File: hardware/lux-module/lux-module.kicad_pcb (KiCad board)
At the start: 2 copper layers, 6 parts, among them J1 Conn_01x04, U1 TSL25911FN

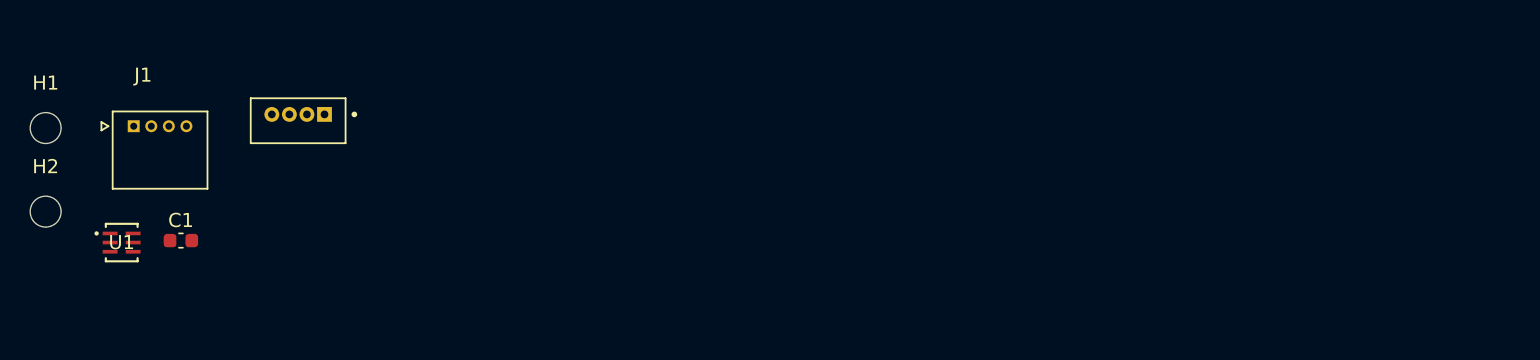
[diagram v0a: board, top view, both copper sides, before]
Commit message: finish lux moudle/ALS
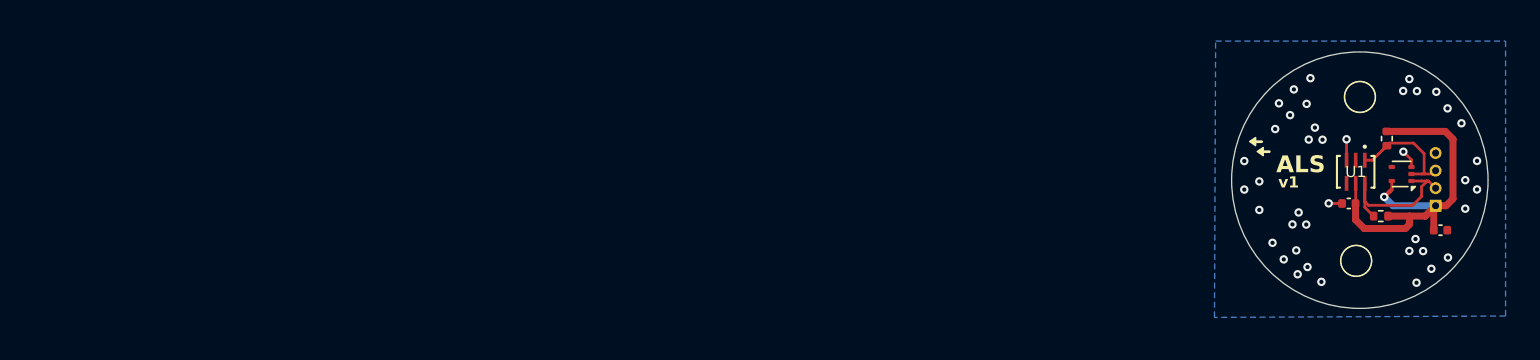
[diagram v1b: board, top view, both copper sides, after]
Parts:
- removed REF**: MOLEX_53047-0460, 53047-0460:MOLEX_53047-0460
- added C2: 10uF, Capacitor_SMD:C_0402_1005Metric, F.Cu at (139.0, 57.7)
- added R1: 2.2k, Resistor_SMD:R_0402_1005Metric, F.Cu at (134.7, 56.7)
- added R2: 2.2k, Resistor_SMD:R_0402_1005Metric, F.Cu at (135.2, 51.1)
- added U2: TPD3E001DRLR, Package_TO_SOT_SMD:SOT-553, F.Cu at (136.2, 53.7)
- C1: footprint Capacitor_SMD:C_0603_1608Metric -> Capacitor_SMD:C_0402_1005Metric
- J1: moved to B.Cu
- moved H2 93.9 mm to (133.2, 48.2)
- moved H1 93.8 mm to (133.0, 59.9)
- moved J1 92.8 mm to (138.6, 55.9), turned to 90 degrees
- moved U1 88.0 mm to (132.9, 53.5), turned to -90 degrees
- moved C1 83.2 mm to (132.4, 55.8), turned to 180 degrees
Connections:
- J1 pad 2: /SCL -> /SDA
- J1 pad 3: /SDA -> /SCL
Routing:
- net +3V3: track 0.00 -> 29.4 mm, vias 0 -> 1
- net /SDA: track 0.00 -> 11.5 mm
- net /SCL: track 0.00 -> 8.79 mm
- net GND: track 0.00 -> 3.78 mm, vias 0 -> 41
- added copper zone on B.Cu, net GND
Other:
- board outline added: 18.3 x 18.3 mm
- board text added: "2026"
- board text added: "ALS"
- board text added: "GND"
- board text added: "JS"
- board text added: "M2"
- board text added: "SCL"
- board text added: "SDA"
- board text added: "VCC"
- board text added: "homectrl"
- board text added: "v1"
- board text added: "|"

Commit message: power circuitry
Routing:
- net /SDA: track 11.5 -> 9.67 mm
- net GND: track 3.78 -> 4.63 mm, vias 41 -> 42
- added copper zone on F.Cu, net GND

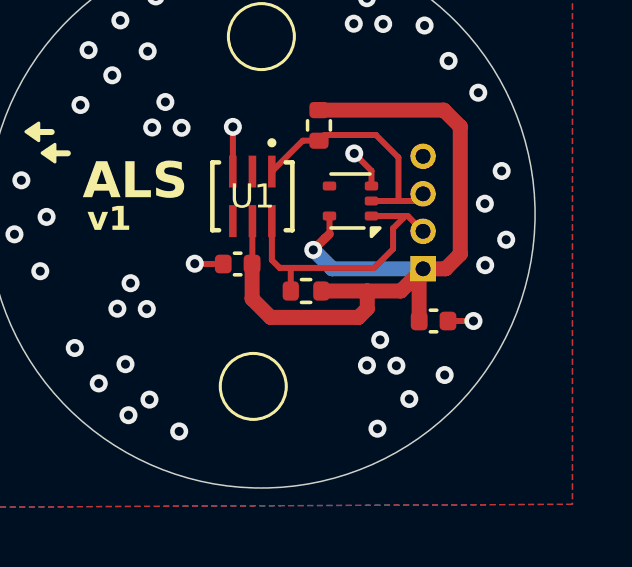
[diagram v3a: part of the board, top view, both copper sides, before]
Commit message: add new caps, add ferrite bead, add MPNs
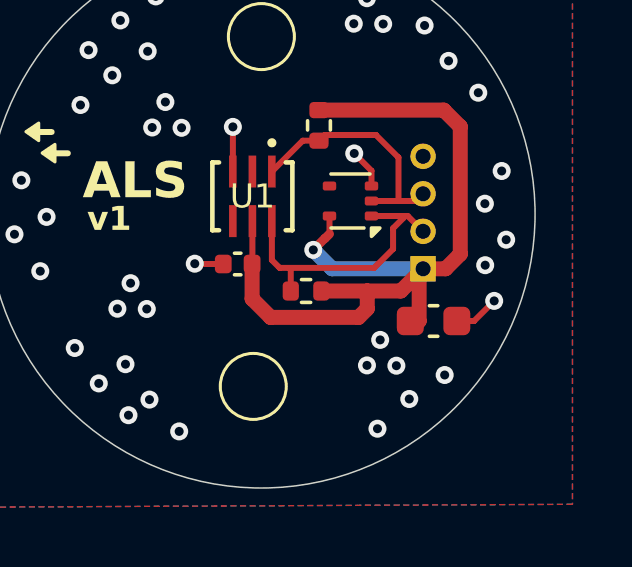
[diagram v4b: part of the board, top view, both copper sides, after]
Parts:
- C2: footprint Capacitor_SMD:C_0402_1005Metric -> Capacitor_SMD:C_0603_1608Metric
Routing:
- net GND: track 4.63 -> 5.59 mm

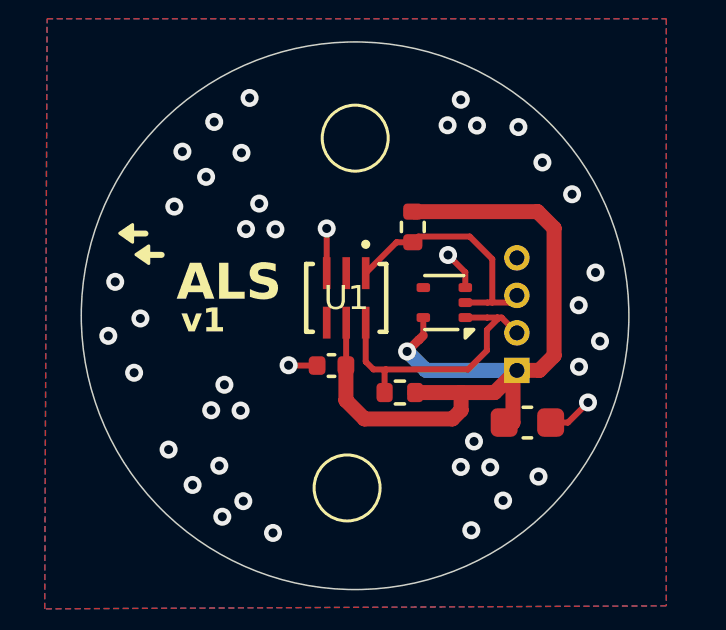
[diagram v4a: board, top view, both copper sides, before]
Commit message: add MPNs and review circuits
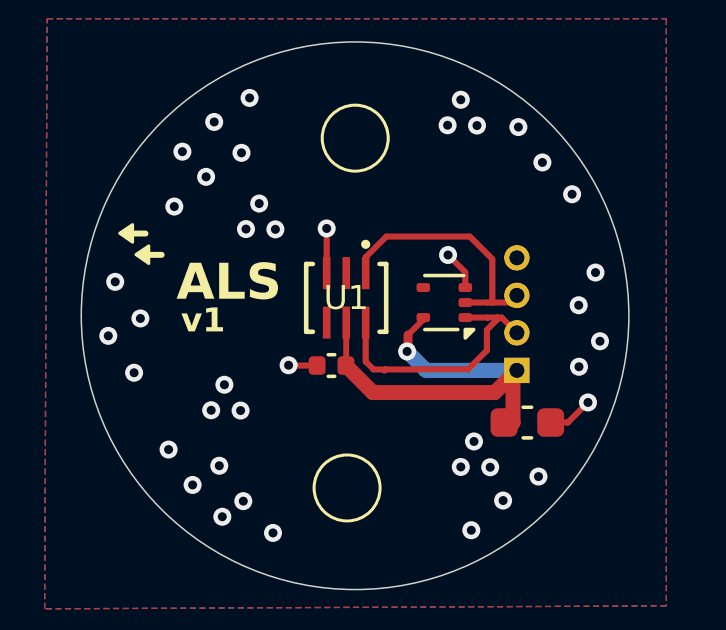
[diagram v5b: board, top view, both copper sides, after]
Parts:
- removed R1, R2: 2.2k, Resistor_SMD:R_0402_1005Metric
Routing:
- net +3V3: track 29.7 -> 15.2 mm
- net /SDA: track 9.67 -> 8.94 mm

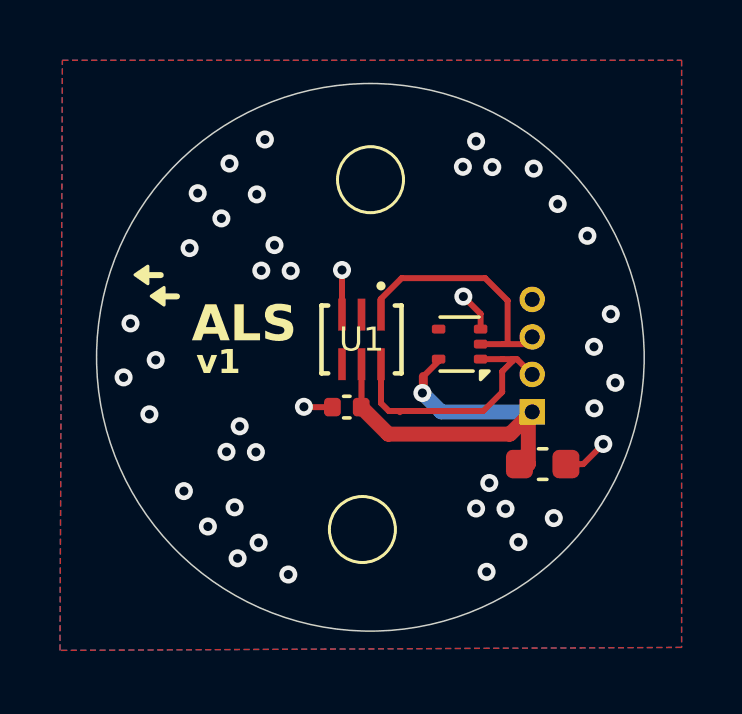
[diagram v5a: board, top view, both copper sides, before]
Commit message: review, add vias & ground pour
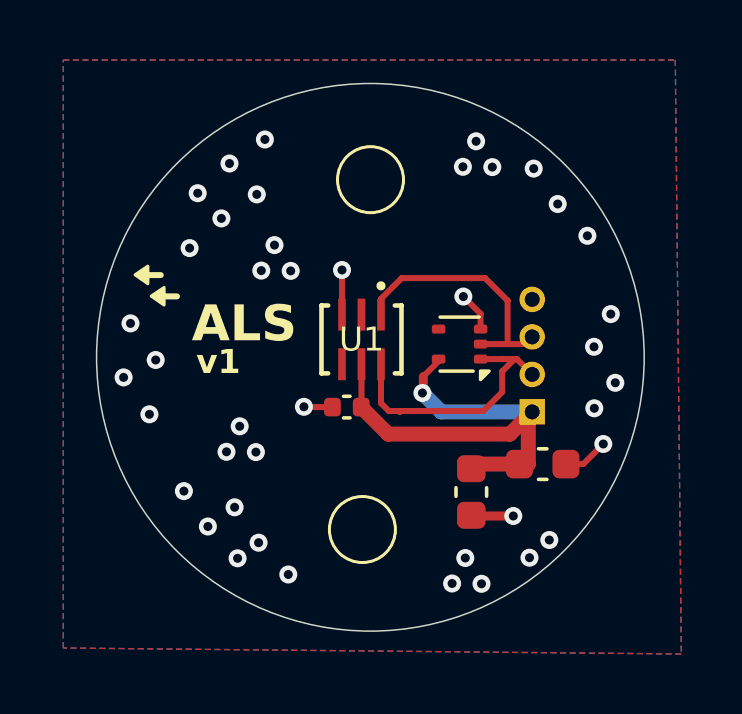
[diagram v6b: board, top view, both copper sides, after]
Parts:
- added Ce: 0.1uF, Capacitor_SMD:C_0603_1608Metric, F.Cu at (136.6, 58.6)
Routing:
- net +3V3: track 15.2 -> 16.9 mm
- net GND: track 5.59 -> 7.00 mm

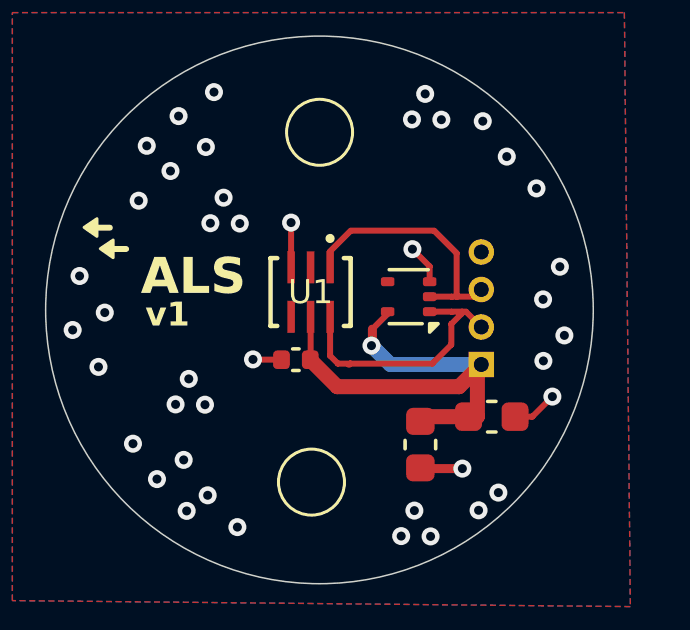
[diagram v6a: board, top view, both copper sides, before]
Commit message: pad clearance & BOM fixes
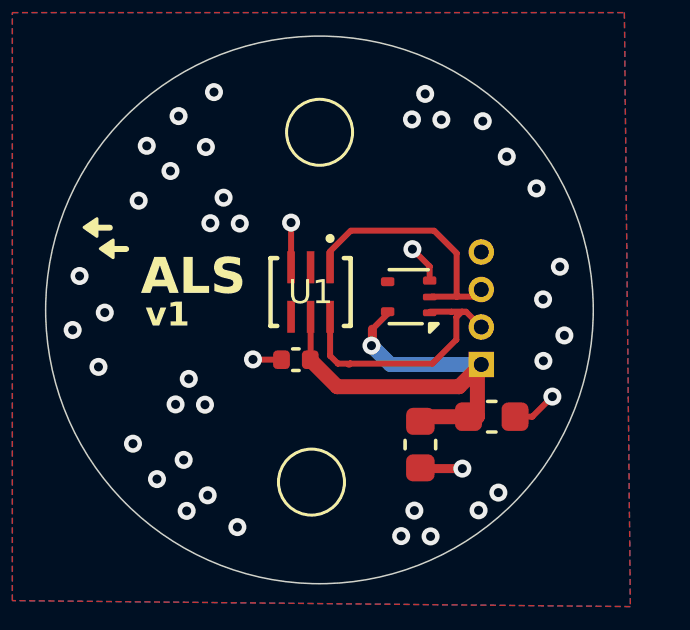
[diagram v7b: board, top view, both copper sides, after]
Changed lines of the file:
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@@
 		)
 		(pad "1" smd roundrect
-			(at -0.7 -0.5 180)
-			(size 0.45 0.3)
+			(at -0.7 -0.5375 180)
+			(size 0.45 0.225)
 			(layers "F.Cu" "F.Paste" "F.Mask")
 			(roundrect_rratio 0.25)
@@
 		)
 		(pad "2" smd roundrect
-			(at -0.7 0 180)
-			(size 0.45 0.3)
+			(at -0.7 -0.0125 180)
+			(size 0.45 0.225)
 			(layers "F.Cu" "F.Paste" "F.Mask")
 			(roundrect_rratio 0.25)
@@
 		)
 		(pad "3" smd roundrect
-			(at -0.7 0.5 180)
-			(size 0.45 0.3)
+			(at -0.7 0.5375 180)
+			(size 0.45 0.275)
 			(layers "F.Cu" "F.Paste" "F.Mask")
 			(roundrect_rratio 0.25)
@@
 			(offset
 				(xyz 2 -3.5 2)
+			)
+			(scale
+				(xyz 1 1 1)
+			)
+			(rotate
+				(xyz 0 0 180)
+			)
+		)
+		(model "C:/Users/Jeevan/Documents/dev/Avionics-23-26/Schematics/upper_lc_board/models/530480410.step"
+			(offset
+				(xyz 2 -3.5 1.5)
 			)
 			(scale
@@
 	)
 	(segment
-		(start 136.335 52.085)
-		(end 136.91 52.66)
-		(width 0.2)
-		(layer "F.Cu")
-		(net 2)
-	)
-	(segment
 		(start 140.33 57.67)
 		(end 139.46 57.67)
@@
 	)
 	(segment
-		(start 136.91 52.66)
-		(end 136.91 53.17)
-		(width 0.2)
-		(layer "F.Cu")
-		(net 2)
-	)
-	(segment
 		(start 136.625 59.4)
 		(end 136.6 59.375)
@@
 	)
 	(segment
+		(start 136.335 52.085)
+		(end 136.91 52.66)
+		(width 0.2)
+		(layer "F.Cu")
+		(net 2)
+	)
+	(segment
+		(start 136.91 52.66)
+		(end 136.91 53.1325)
+		(width 0.2)
+		(layer "F.Cu")
+		(net 2)
+	)
+	(segment
 		(start 132.290028 51.190028)
 		(end 132.29 51.19)
@@
 	)
 	(segment
+		(start 134.26 55.9)
+		(end 137 55.9)
+		(width 0.2)
+		(layer "F.Cu")
+		(net 3)
+	)
+	(segment
+		(start 137 55.9)
+		(end 137.8 55.1)
+		(width 0.2)
+		(layer "F.Cu")
+		(net 3)
+	)
+	(segment
+		(start 137.8 54.35)
+		(end 137.98 54.17)
+		(width 0.2)
+		(layer "F.Cu")
+		(net 3)
+	)
+	(segment
 		(start 136.91 54.17)
 		(end 137.64 54.17)
@@
 	)
 	(segment
-		(start 137 55.9)
-		(end 137.63 55.27)
-		(width 0.2)
-		(layer "F.Cu")
-		(net 3)
-	)
-	(segment
-		(start 137.98 54.23)
-		(end 137.98 54.17)
-		(width 0.2)
-		(layer "F.Cu")
-		(net 3)
-	)
-	(segment
 		(start 133.59 55.64)
 		(end 133.85 55.9)
@@
 	)
 	(segment
-		(start 137.63 55.27)
-		(end 137.63 54.58)
-		(width 0.2)
-		(layer "F.Cu")
-		(net 3)
-	)
-	(segment
 		(start 133.85 55.9)
 		(end 134.26 55.9)
@@
 	)
 	(segment
-		(start 134.26 55.9)
-		(end 137 55.9)
-		(width 0.2)
-		(layer "F.Cu")
-		(net 3)
-	)
-	(segment
 		(start 133.59 54.34)
 		(end 133.59 55.64)
@@
 	)
 	(segment
-		(start 137.63 54.58)
-		(end 137.98 54.23)
+		(start 137.8 55.1)
+		(end 137.8 54.35)
 		(width 0.2)
 		(layer "F.Cu")
@@
 	)
 	(segment
-		(start 137.65 53.67)
-		(end 138.39 53.67)
-		(width 0.2)
-		(layer "F.Cu")
-		(net 4)
-	)
-	(segment
 		(start 138.39 53.67)
 		(end 138.63 53.43)
@@
 	)
 	(segment
-		(start 136.91 53.67)
-		(end 137.65 53.67)
-		(width 0.2)
-		(layer "F.Cu")
+		(start 136.9475 53.67)
+		(end 138.39 53.67)
+		(width 0.2)
+		(layer "F.Cu")

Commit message: swap connector in progress
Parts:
- added C3: 0.1uF, Capacitor_SMD:C_0603_1608Metric, F.Cu at (79.6, 55.9)
- J1: footprint 530480410:MOLEX_530480410 -> S04B_PASK_2:CONN4_S04B-PASK_JST
- moved J1 4.88 mm to (138.6, 51.1), turned to -90 degrees
- moved H1 2.34 mm to (132.9, 62.2)
- moved H2 2.14 mm to (133.2, 46.0)
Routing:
- removed copper zone on B.Cu, net GND
- removed copper zone on F.Cu, net GND
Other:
- board size 18.3 x 18.3 mm -> 21.6 x 21.6 mm
